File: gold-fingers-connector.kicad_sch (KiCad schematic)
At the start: 128 parts, among them J2 Socket_DC-SCM-2.1_2x84_Rev-1-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

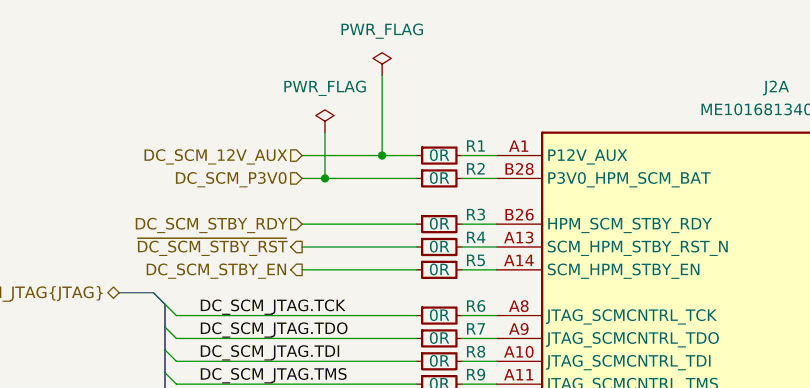
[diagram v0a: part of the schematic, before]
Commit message: [#100720] Finish schematic, clean ERC
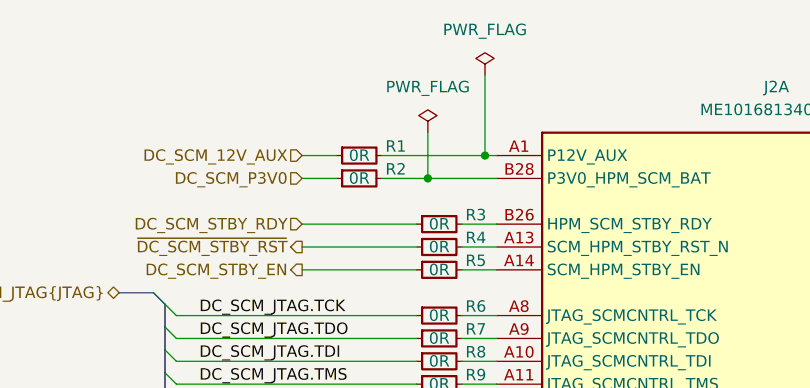
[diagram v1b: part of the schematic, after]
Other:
- moved on the sheet: R1, R2
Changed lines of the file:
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@@
 	)
 	(junction
-		(at 64.77 45.72)
+		(at 76.2 45.72)
 		(diameter 0)
 		(color 0 0 0 0)
 	)
 	(junction
-		(at 71.12 43.18)
+		(at 82.55 43.18)
 		(diameter 0)
 		(color 0 0 0 0)
@@
 	(wire
 		(pts
-			(xy 62.23 43.18) (xy 71.12 43.18)
+			(xy 62.23 43.18) (xy 66.04 43.18)
 		)
 		(stroke
@@
 	(wire
 		(pts
-			(xy 64.77 40.64) (xy 64.77 45.72)
+			(xy 76.2 40.64) (xy 76.2 45.72)
 		)
 		(stroke
@@
 	(wire
 		(pts
+			(xy 76.2 45.72) (xy 83.82 45.72)
+		)
+		(stroke
+			(width 0)
+			(type default)
+		)
+	)
+	(wire
+		(pts
 			(xy 80.01 149.86) (xy 83.82 149.86)
 		)
@@
 	(wire
 		(pts
-			(xy 80.01 45.72) (xy 83.82 45.72)
+			(xy 71.12 45.72) (xy 76.2 45.72)
 		)
 		(stroke
@@
 	(wire
 		(pts
-			(xy 62.23 45.72) (xy 64.77 45.72)
+			(xy 62.23 45.72) (xy 66.04 45.72)
 		)
 		(stroke
@@
 	(wire
 		(pts
-			(xy 80.01 43.18) (xy 83.82 43.18)
+			(xy 71.12 43.18) (xy 82.55 43.18)
 		)
 		(stroke
@@
 	(wire
 		(pts
+			(xy 82.55 43.18) (xy 83.82 43.18)
+		)
+		(stroke
+			(width 0)
+			(type default)
+		)
+	)
+	(wire
+		(pts
 			(xy 152.4 48.26) (xy 158.75 48.26)
 		)
@@
 	(wire
 		(pts
-			(xy 64.77 45.72) (xy 74.93 45.72)
-		)
-		(stroke
-			(width 0)
-			(type default)
-		)
-	)
-	(wire
-		(pts
 			(xy 80.01 160.02) (xy 83.82 160.02)
 		)
@@
 	(wire
 		(pts
-			(xy 71.12 43.18) (xy 74.93 43.18)
-		)
-		(stroke
-			(width 0)
-			(type default)
-		)
-	)
-	(wire
-		(pts
 			(xy 63.5 78.74) (xy 74.93 78.74)
 		)
@@
 	(wire
 		(pts
-			(xy 71.12 34.29) (xy 71.12 43.18)
+			(xy 82.55 34.29) (xy 82.55 43.18)
 		)
 		(stroke
@@
 	(symbol
 		(lib_id "antmicropower:PWR_FLAG")
-		(at 71.12 34.29 0)
+		(at 82.55 34.29 0)
 		(unit 1)
 		(body_style 1)
@@
 		(fields_autoplaced yes)
 		(property "Reference" "#FLG02"
-			(at 71.12 32.385 0)
+			(at 82.55 32.385 0)
 			(hide yes)
 			(show_name no)
@@
 		)
 		(property "Value" "PWR_FLAG"
-			(at 71.12 29.21 0)
+			(at 82.55 29.21 0)
 			(show_name no)
 			(do_not_autoplace no)
@@
 		)
 		(property "Footprint" ""
-			(at 71.12 34.29 0)
+			(at 82.55 34.29 0)
 			(hide yes)
 			(show_name no)
@@
 		)
 		(property "Datasheet" ""
-			(at 71.12 34.29 0)
+			(at 82.55 34.29 0)
 			(hide yes)
 			(show_name no)
@@
 		)
 		(property "Description" ""
-			(at 71.12 36.83 0)
+			(at 82.55 36.83 0)
 			(hide yes)
 			(show_name no)
@@
 	(symbol
 		(lib_id "antmicroResistors0402:R_0R_0402")
-		(at 74.93 45.72 0)
+		(at 66.04 45.72 0)
 		(unit 1)
 		(body_style 1)
@@
 		(dnp no)
 		(property "Reference" "R2"
-			(at 81.534 44.704 0)
+			(at 72.644 44.704 0)
 			(show_name no)
 			(do_not_autoplace no)
@@
 		)
 		(property "Value" "R_0R_0402"
-			(at 95.25 58.42 0)
+			(at 86.36 58.42 0)
 			(hide yes)
 			(show_name no)
@@
 		)
 		(property "Footprint" "antmicro-footprints:R_0402_1005Metric"
-			(at 95.25 60.96 0)
+			(at 86.36 60.96 0)
 			(hide yes)
 			(show_name no)
@@
 		)
 		(property "Datasheet" "https://industrial.panasonic.com/cdbs/www-data/pdf/RDA0000/AOA0000C301.pdf"
-			(at 95.25 63.5 0)
+			(at 86.36 63.5 0)
 			(hide yes)
 			(show_name no)
@@
 		)
 		(property "Description" "SMD Chip Resistor, Jumper, 0 ohm, 100 mW, 0402 [1005 Metric], Thick Film, General Purpose"
-			(at 74.93 45.72 0)
+			(at 66.04 45.72 0)
 			(hide yes)
 			(show_name no)
@@
 		)
 		(property "MPN" "ERJ2GE0R00X"
-			(at 95.25 66.04 0)
+			(at 86.36 66.04 0)
 			(hide yes)
 			(show_name no)
@@
 		)
 		(property "Manufacturer" "Panasonic"
-			(at 95.25 68.58 0)
+			(at 86.36 68.58 0)
 			(hide yes)
 			(show_name no)
@@
 		)
 		(property "License" "Apache-2.0"
-			(at 95.25 71.12 0)
+			(at 86.36 71.12 0)
 			(hide yes)
 			(show_name no)
@@
 		)
 		(property "Author" "Antmicro"
-			(at 95.25 73.66 0)
+			(at 86.36 73.66 0)
 			(hide yes)
 			(show_name no)
@@
 		)
 		(property "Val" "0R"
-			(at 77.47 45.72 0)
+			(at 68.58 45.72 0)
 			(show_name no)
 			(do_not_autoplace no)
@@
 		)
 		(property "Tolerance" ""
-			(at 95.25 55.88 0)
+			(at 86.36 55.88 0)
 			(hide yes)
 			(show_name no)
@@
 		)
 		(property "Current" "1A"
-			(at 95.25 76.2 0)
+			(at 86.36 76.2 0)
 			(hide yes)
 			(show_name no)
@@
 	(symbol
 		(lib_id "antmicropower:PWR_FLAG")
-		(at 64.77 40.64 0)
+		(at 76.2 40.64 0)
 		(unit 1)
 		(body_style 1)
@@
 		(fields_autoplaced yes)
 		(property "Reference" "#FLG05"
-			(at 64.77 38.735 0)
+			(at 76.2 38.735 0)
 			(hide yes)
 			(show_name no)
@@
 		)
 		(property "Value" "PWR_FLAG"
-			(at 64.77 35.56 0)
+			(at 76.2 35.56 0)
 			(show_name no)
 			(do_not_autoplace no)
@@
 		)
 		(property "Footprint" ""
-			(at 64.77 40.64 0)
+			(at 76.2 40.64 0)
 			(hide yes)
 			(show_name no)
@@
 		)
 		(property "Datasheet" ""
-			(at 64.77 40.64 0)
+			(at 76.2 40.64 0)
 			(hide yes)
 			(show_name no)
@@
 		)
 		(property "Description" ""
-			(at 64.77 43.18 0)
+			(at 76.2 43.18 0)
 			(hide yes)
 			(show_name no)
@@
 	(symbol
 		(lib_id "antmicroResistors0402:R_0R_0402")
-		(at 74.93 43.18 0)
+		(at 66.04 43.18 0)
 		(unit 1)
 		(body_style 1)
@@
 		(dnp no)
 		(property "Reference" "R1"
-			(at 81.534 42.164 0)
+			(at 72.644 42.164 0)
 			(show_name no)
 			(do_not_autoplace no)
@@
 		)
 		(property "Value" "R_0R_0402"
-			(at 95.25 55.88 0)
+			(at 86.36 55.88 0)
 			(hide yes)
 			(show_name no)
@@
 		)
 		(property "Footprint" "antmicro-footprints:R_0402_1005Metric"
-			(at 95.25 58.42 0)
+			(at 86.36 58.42 0)
 			(hide yes)
 			(show_name no)
@@
 		)
 		(property "Datasheet" "https://industrial.panasonic.com/cdbs/www-data/pdf/RDA0000/AOA0000C301.pdf"
-			(at 95.25 60.96 0)
+			(at 86.36 60.96 0)
 			(hide yes)
 			(show_name no)
@@
 		)
 		(property "Description" "SMD Chip Resistor, Jumper, 0 ohm, 100 mW, 0402 [1005 Metric], Thick Film, General Purpose"
-			(at 74.93 43.18 0)
+			(at 66.04 43.18 0)
 			(hide yes)
 			(show_name no)
@@
 		)
 		(property "MPN" "ERJ2GE0R00X"
-			(at 95.25 63.5 0)
+			(at 86.36 63.5 0)
 			(hide yes)
 			(show_name no)
@@
 		)
 		(property "Manufacturer" "Panasonic"
-			(at 95.25 66.04 0)
+			(at 86.36 66.04 0)
 			(hide yes)
 			(show_name no)
@@
 		)
 		(property "License" "Apache-2.0"
-			(at 95.25 68.58 0)
+			(at 86.36 68.58 0)
 			(hide yes)
 			(show_name no)
@@
 		)
 		(property "Author" "Antmicro"
-			(at 95.25 71.12 0)
+			(at 86.36 71.12 0)
 			(hide yes)
 			(show_name no)
@@
 		)
 		(property "Val" "0R"
-			(at 77.47 43.18 0)
+			(at 68.58 43.18 0)
 			(show_name no)
 			(do_not_autoplace no)
@@
 		)
 		(property "Tolerance" ""
-			(at 95.25 53.34 0)
+			(at 86.36 53.34 0)
 			(hide yes)
 			(show_name no)
@@
 		)
 		(property "Current" "1A"
-			(at 95.25 73.66 0)
+			(at 86.36 73.66 0)
 			(hide yes)
 			(show_name no)

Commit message: [#100720] Reannotate
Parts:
- renumbered J2 to J1, R103 to R100, R104 to R101, R105 to R102, R106 to R103, R107 to R104, R108 to R105, R109 to R106, R110 to R107, R111 to R108, R112 to R109, R113 to R110, R114 to R111, R115 to R112, R116 to R113, R117 to R114, R118 to R115, R119 to R116, R120 to R117, R121 to R118, R122 to R119, R13 to R12, R123 to R120, R124 to R121, R125 to R122, R126 to R123, R127 to R124, R128 to R125, R129 to R126, R130 to R127, R14 to R13, R15 to R14, R16 to R15, R18 to R16, R19 to R17, R20 to R18, R21 to R19, R22 to R20, R23 to R21, R24 to R22, R25 to R23, R26 to R24, R27 to R25, R28 to R26, R29 to R27, R30 to R28, R31 to R29, R32 to R30, R33 to R31, R34 to R32, R35 to R33, R36 to R34, R37 to R35, R38 to R36, R39 to R37, R40 to R38, R41 to R39, R42 to R40, R43 to R41, R44 to R42, R45 to R43, R46 to R44, R47 to R45, R48 to R46, R49 to R47, R50 to R48, R51 to R49, R52 to R50, R53 to R51, R54 to R52, R55 to R53, R57 to R54, R58 to R55, R59 to R56, R60 to R57, R61 to R58, R62 to R59, R63 to R60, R64 to R61, R65 to R62, R66 to R63, R67 to R64, R68 to R65, R69 to R66, R70 to R67, R71 to R68, R72 to R69, R73 to R70, R74 to R71, R75 to R72, R76 to R73, R77 to R74, R78 to R75, R79 to R76, R80 to R77, R81 to R78, R82 to R79, R83 to R80, R84 to R81, R85 to R82, R86 to R83, R87 to R84, R88 to R85, R89 to R86, R90 to R87, R91 to R88, R92 to R89, R93 to R90, R94 to R91, R95 to R92, R96 to R93, R97 to R94, R98 to R95, R99 to R96, R100 to R97, R101 to R98, R102 to R99

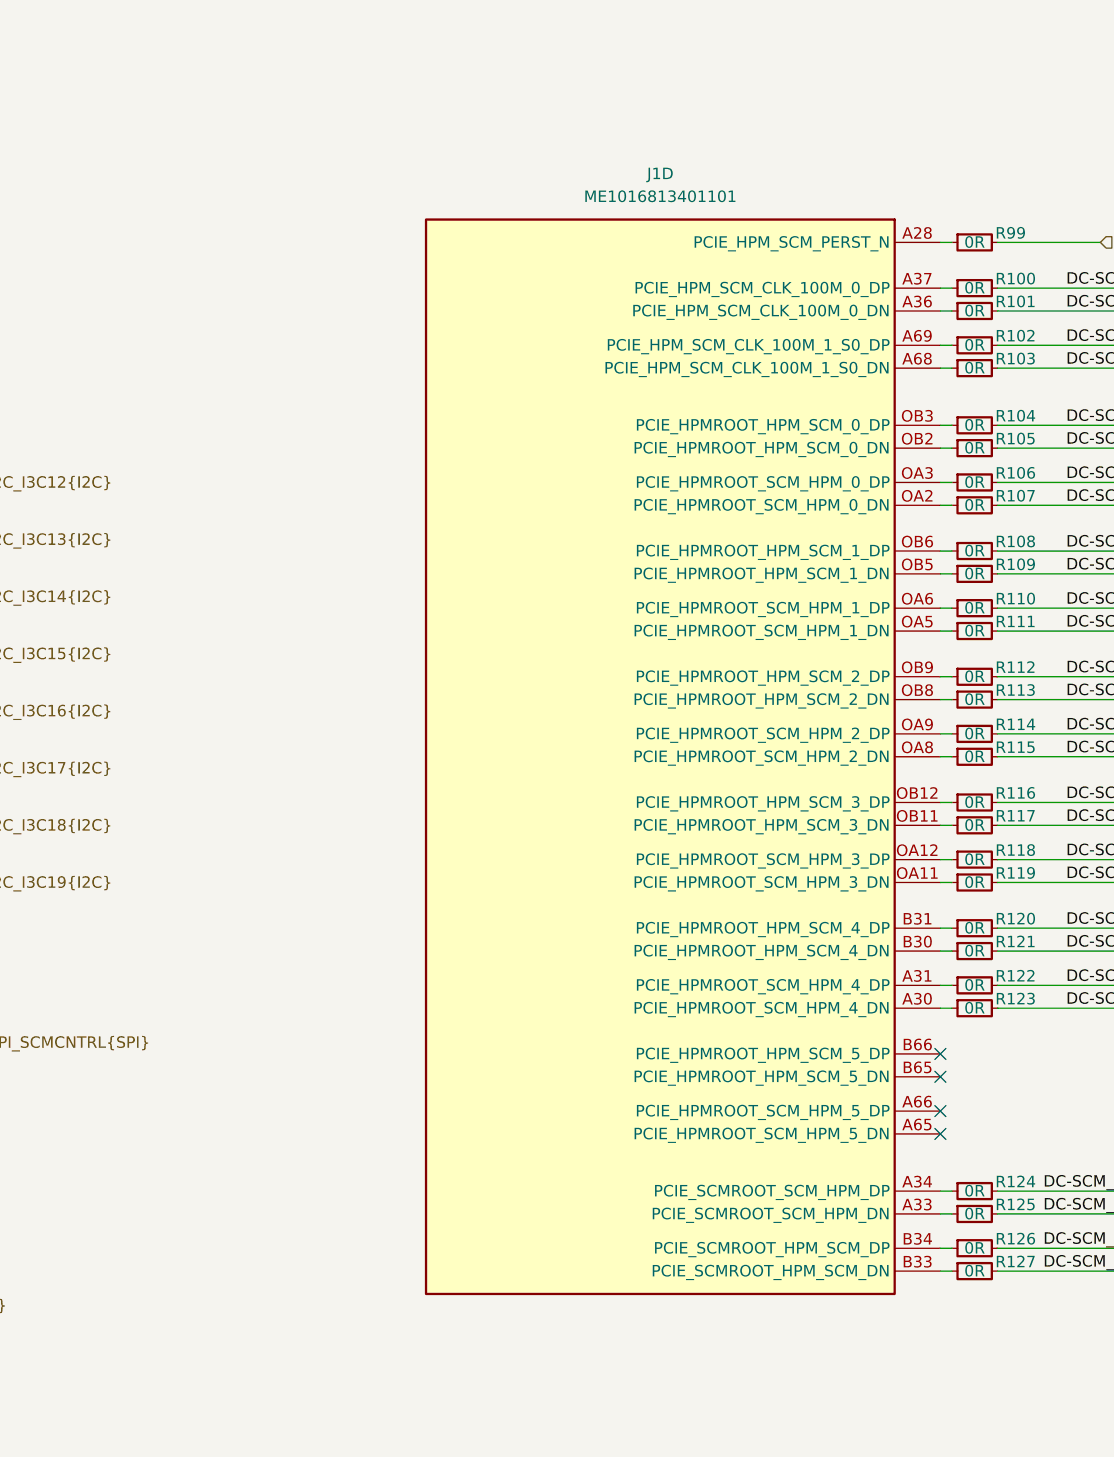
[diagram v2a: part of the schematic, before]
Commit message: [#100720] Start routing high speeds
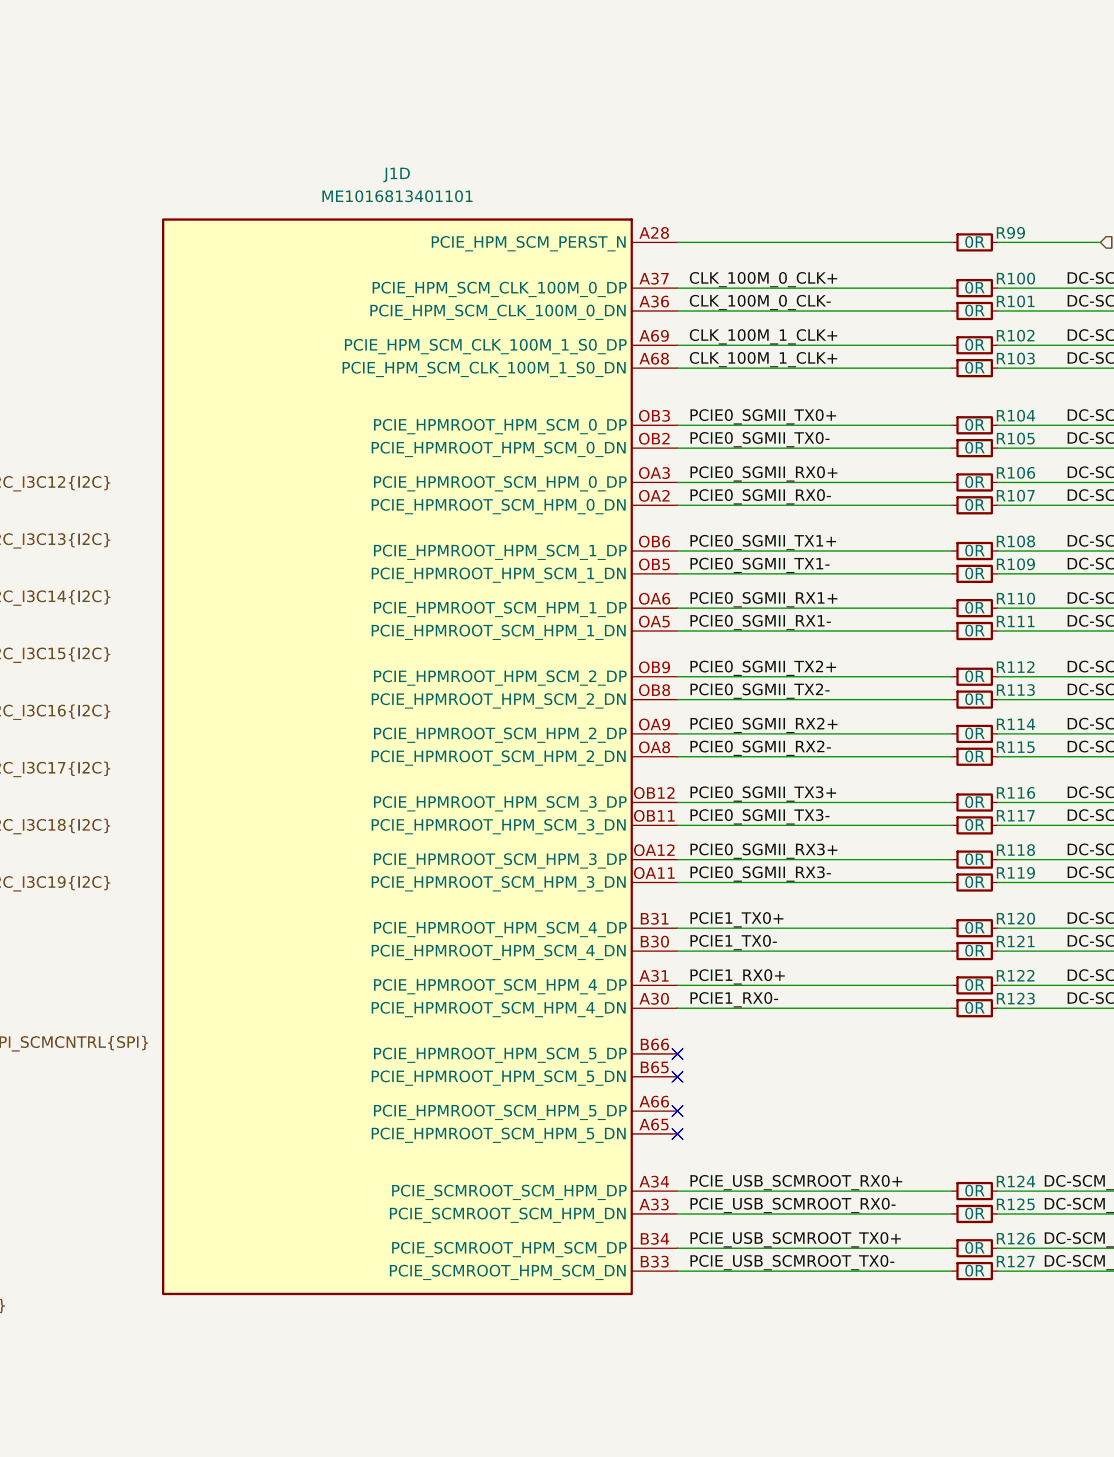
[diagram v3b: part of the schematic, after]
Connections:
- net PCIE0_SGMII_RX1-: now reaches J1.OA5 (PCIE_HPMROOT_SCM_HPM_1_DN), R111.1
- net PCIE1_RX0-: now reaches J1.A30 (PCIE_HPMROOT_SCM_HPM_4_DN), R123.1
- net PCIE_USB_SCMROOT_TX0-: now reaches J1.B33 (PCIE_SCMROOT_HPM_SCM_DN), R127.1
- net PCIE0_SGMII_TX3+: now reaches J1.OB12 (PCIE_HPMROOT_HPM_SCM_3_DP), R116.1
- net PCIE0_SGMII_TX3-: now reaches J1.OB11 (PCIE_HPMROOT_HPM_SCM_3_DN), R117.1
- net CLK_100M_1_CLK+: now reaches J1.A68 (PCIE_HPM_SCM_CLK_100M_1_S0_DN), R103.1
- net CLK_100M_1_CLK+: now also J1.A69 (PCIE_HPM_SCM_CLK_100M_1_S0_DP), R102.1
- net PCIE1_RX0+: now reaches J1.A31 (PCIE_HPMROOT_SCM_HPM_4_DP), R122.1
- net PCIE_USB_SCMROOT_RX0-: now reaches J1.A33 (PCIE_SCMROOT_SCM_HPM_DN), R125.1
- net PCIE_USB_SCMROOT_RX0+: now reaches J1.A34 (PCIE_SCMROOT_SCM_HPM_DP), R124.1
- net CLK_100M_0_CLK-: now reaches J1.A36 (PCIE_HPM_SCM_CLK_100M_0_DN), R101.1
- net CLK_100M_0_CLK+: now reaches J1.A37 (PCIE_HPM_SCM_CLK_100M_0_DP), R100.1
- net PCIE1_TX0-: now reaches J1.B30 (PCIE_HPMROOT_HPM_SCM_4_DN), R121.1
- net PCIE1_TX0+: now reaches J1.B31 (PCIE_HPMROOT_HPM_SCM_4_DP), R120.1
- net PCIE_USB_SCMROOT_TX0+: now reaches J1.B34 (PCIE_SCMROOT_HPM_SCM_DP), R126.1
- net PCIE0_SGMII_RX3-: now reaches J1.OA11 (PCIE_HPMROOT_SCM_HPM_3_DN), R119.1
- net PCIE0_SGMII_RX3+: now reaches J1.OA12 (PCIE_HPMROOT_SCM_HPM_3_DP), R118.1
- net PCIE0_SGMII_RX0-: now reaches J1.OA2 (PCIE_HPMROOT_SCM_HPM_0_DN), R107.1
- net PCIE0_SGMII_RX0+: now reaches J1.OA3 (PCIE_HPMROOT_SCM_HPM_0_DP), R106.1
- net PCIE0_SGMII_RX1+: now reaches J1.OA6 (PCIE_HPMROOT_SCM_HPM_1_DP), R110.1
- net PCIE0_SGMII_RX2-: now reaches J1.OA8 (PCIE_HPMROOT_SCM_HPM_2_DN), R115.1
- net PCIE0_SGMII_RX2+: now reaches J1.OA9 (PCIE_HPMROOT_SCM_HPM_2_DP), R114.1
- net PCIE0_SGMII_TX0-: now reaches J1.OB2 (PCIE_HPMROOT_HPM_SCM_0_DN), R105.1
- net PCIE0_SGMII_TX0+: now reaches J1.OB3 (PCIE_HPMROOT_HPM_SCM_0_DP), R104.1
- net PCIE0_SGMII_TX1-: now reaches J1.OB5 (PCIE_HPMROOT_HPM_SCM_1_DN), R109.1
- net PCIE0_SGMII_TX1+: now reaches J1.OB6 (PCIE_HPMROOT_HPM_SCM_1_DP), R108.1
- net PCIE0_SGMII_TX2-: now reaches J1.OB8 (PCIE_HPMROOT_HPM_SCM_2_DN), R113.1
- net PCIE0_SGMII_TX2+: now reaches J1.OB9 (PCIE_HPMROOT_HPM_SCM_2_DP), R112.1
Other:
- moved on the sheet: J1D
